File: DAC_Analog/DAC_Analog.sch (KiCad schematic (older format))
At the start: 17 parts

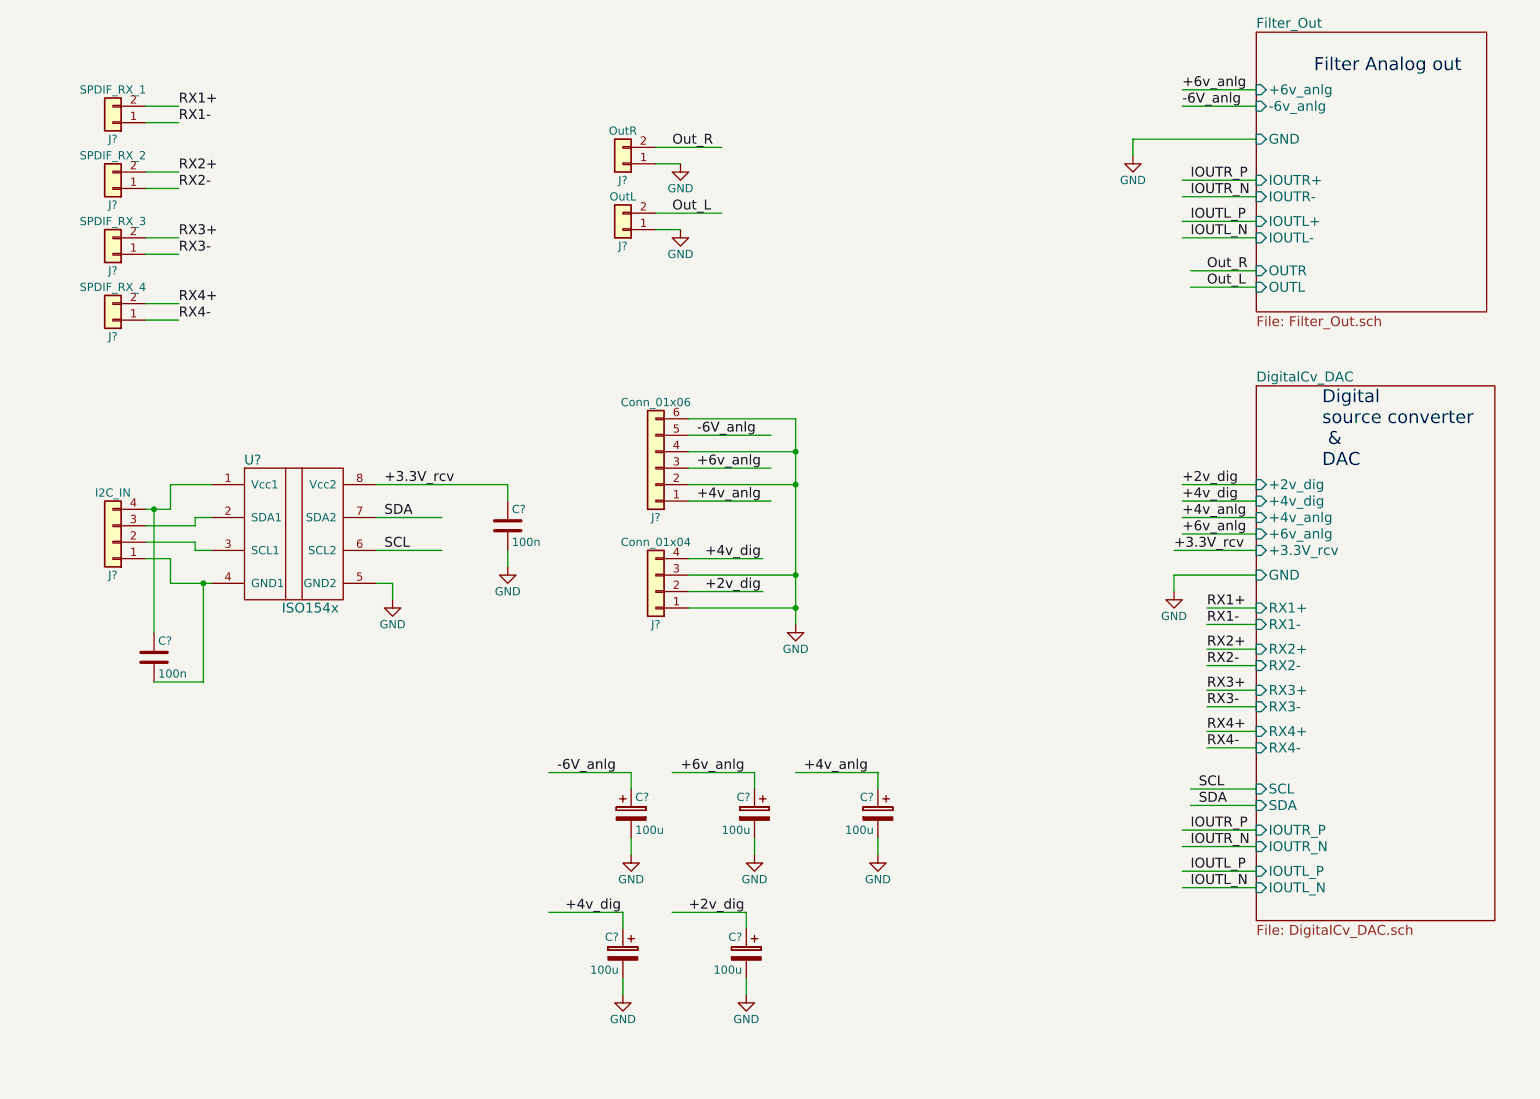
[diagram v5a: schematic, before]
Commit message: Footprint assignment ok
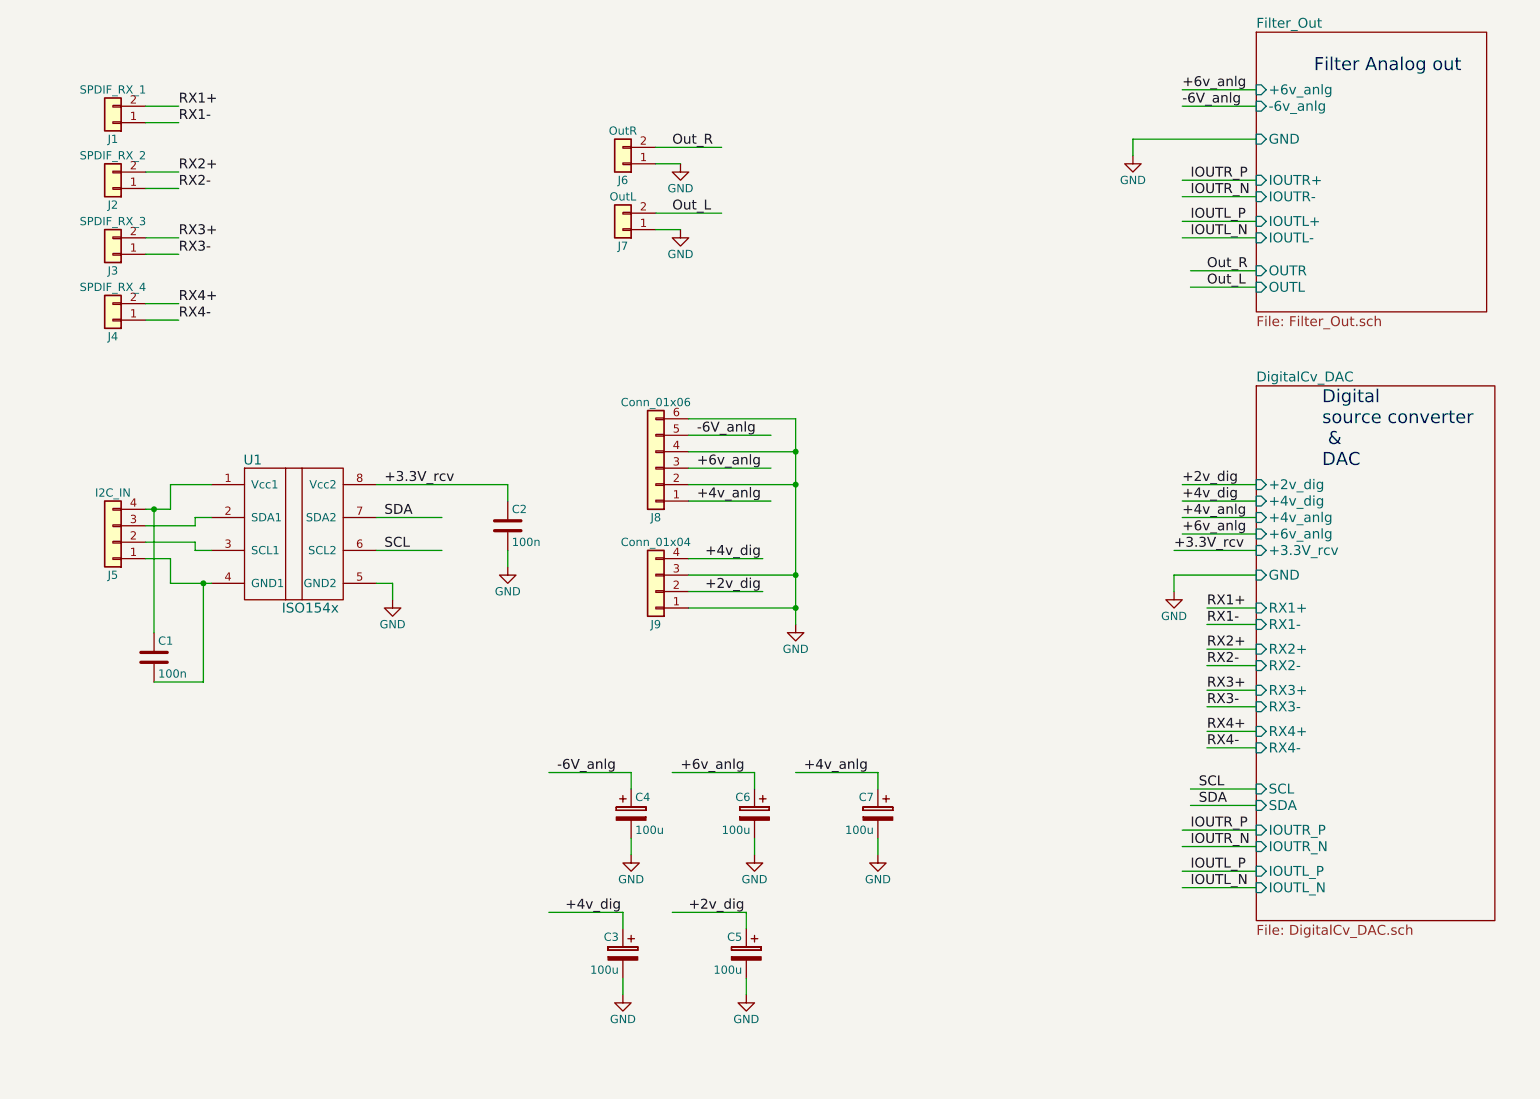
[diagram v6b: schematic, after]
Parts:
- J1, J2, J3, J4: renamed from J?; footprint (none) -> Yame_library:HE10_14-2C-2.54-MR
- J6: renamed from J?; footprint Housings_DIP:DIP-6_W10.16mm_LongPads -> Yame_library:HE10_14-2C-2.54-MR
- gave numbers to parts that had none: 12
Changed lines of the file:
@@
 Digital \nsource converter\n &\nDAC
 $Comp
-L ISO154x U?
+L ISO154x U1
 U 1 1 59C5CEDC
 P 2400 3750
-F 0 "U?" H 2150 4200 60  0000 C CNN
+F 0 "U1" H 2150 4200 60  0000 C CNN
 F 1 "ISO154x" H 2500 3300 60  0000 C CNN
 F 2 "Housings_SOIC:SOIC-8_3.9x4.9mm_Pitch1.27mm" H 2400 3750 60  0001 C CNN
@@
 $EndComp
 $Comp
-L Conn_01x02 J?
+L Conn_01x02 J1
 U 1 1 59C96FBC
 P 1300 1250
-F 0 "J?" H 1300 1350 50  0000 C CNN
+F 0 "J1" H 1300 1350 50  0000 C CNN
 F 1 "SPDIF_RX_1" H 1300 1050 50  0000 C CNN
-F 2 "" H 1300 1250 50  0001 C CNN
+F 2 "Yame_library:HE10_14-2C-2.54-MR" H 1300 1250 50  0001 C CNN
 F 3 "" H 1300 1250 50  0001 C CNN
 	1    1300 1250
@@
 $EndComp
 $Comp
-L Conn_01x02 J?
+L Conn_01x02 J2
 U 1 1 59C970A3
 P 1300 1650
-F 0 "J?" H 1300 1750 50  0000 C CNN
+F 0 "J2" H 1300 1750 50  0000 C CNN
 F 1 "SPDIF_RX_2" H 1300 1450 50  0000 C CNN
-F 2 "" H 1300 1650 50  0001 C CNN
+F 2 "Yame_library:HE10_14-2C-2.54-MR" H 1300 1650 50  0001 C CNN
 F 3 "" H 1300 1650 50  0001 C CNN
 	1    1300 1650
@@
 $EndComp
 $Comp
-L Conn_01x02 J?
+L Conn_01x02 J3
 U 1 1 59C970DE
 P 1300 2050
-F 0 "J?" H 1300 2150 50  0000 C CNN
+F 0 "J3" H 1300 2150 50  0000 C CNN
 F 1 "SPDIF_RX_3" H 1300 1850 50  0000 C CNN
-F 2 "" H 1300 2050 50  0001 C CNN
+F 2 "Yame_library:HE10_14-2C-2.54-MR" H 1300 2050 50  0001 C CNN
 F 3 "" H 1300 2050 50  0001 C CNN
 	1    1300 2050
@@
 $EndComp
 $Comp
-L Conn_01x02 J?
+L Conn_01x02 J4
 U 1 1 59C97110
 P 1300 2450
-F 0 "J?" H 1300 2550 50  0000 C CNN
+F 0 "J4" H 1300 2550 50  0000 C CNN
 F 1 "SPDIF_RX_4" H 1300 2250 50  0000 C CNN
-F 2 "" H 1300 2450 50  0001 C CNN
+F 2 "Yame_library:HE10_14-2C-2.54-MR" H 1300 2450 50  0001 C CNN
 F 3 "" H 1300 2450 50  0001 C CNN
 	1    1300 2450
@@
 $EndComp
 $Comp
-L Conn_01x04 J?
+L Conn_01x04 J9
 U 1 1 59C971D1
 P 4600 4100
-F 0 "J?" H 4600 4300 50  0000 C CNN
+F 0 "J9" H 4600 4300 50  0000 C CNN
 F 1 "Conn_01x04" H 4600 3800 50  0000 C CNN
 F 2 "Yame_library:HE10_14-4C-2.54-MR" H 4600 4100 50  0001 C CNN
@@
 $EndComp
 $Comp
-L Conn_01x06 J?
+L Conn_01x06 J8
 U 1 1 59C972F4
 P 4600 3350
-F 0 "J?" H 4600 3650 50  0000 C CNN
+F 0 "J8" H 4600 3650 50  0000 C CNN
 F 1 "Conn_01x06" H 4600 2950 50  0000 C CNN
 F 2 "Yame_library:HE10_14-6C-2.54-MR" H 4600 3350 50  0001 C CNN
@@
 $EndComp
 $Comp
-L Conn_01x04 J?
+L Conn_01x04 J5
 U 1 1 59C97424
 P 1300 3800
-F 0 "J?" H 1300 4000 50  0000 C CNN
+F 0 "J5" H 1300 4000 50  0000 C CNN
 F 1 "I2C_IN" H 1300 3500 50  0000 C CNN
 F 2 "Yame_library:HE10_14-4C-2.54-MR" H 1300 3800 50  0001 C CNN
@@
 $EndComp
 $Comp
-L Conn_01x02 J?
+L Conn_01x02 J6
 U 1 1 59C976CC
 P 4400 1500
-F 0 "J?" H 4400 1600 50  0000 C CNN
+F 0 "J6" H 4400 1600 50  0000 C CNN
 F 1 "OutR" H 4400 1300 50  0000 C CNN
-F 2 "Housings_DIP:DIP-6_W10.16mm_LongPads" H 4400 1500 50  0001 C CNN
+F 2 "Yame_library:HE10_14-2C-2.54-MR" H 4400 1500 50  0001 C CNN
 F 3 "" H 4400 1500 50  0001 C CNN
 	1    4400 1500
@@
 $EndComp
 $Comp
-L Conn_01x02 J?
+L Conn_01x02 J7
 U 1 1 59C976D2
 P 4400 1900
-F 0 "J?" H 4400 2000 50  0000 C CNN
+F 0 "J7" H 4400 2000 50  0000 C CNN
 F 1 "OutL" H 4400 1700 50  0000 C CNN
 F 2 "Yame_library:HE10_14-2C-2.54-MR" H 4400 1900 50  0001 C CNN
@@
 	1650 4050 1900 4050
 $Comp
-L GND #PWR?
+L GND #PWR01
 U 1 1 59CB983A
 P 3000 4150
-F 0 "#PWR?" H 3000 3900 50  0001 C CNN
+F 0 "#PWR01" H 3000 3900 50  0001 C CNN
 F 1 "GND" H 3000 4000 50  0000 C CNN
 F 2 "" H 3000 4150 50  0001 C CNN
@@
 	7850 2250 8250 2250
 $Comp
-L GND #PWR?
+L GND #PWR02
 U 1 1 59CBC1FC
 P 7750 4100
-F 0 "#PWR?" H 7750 3850 50  0001 C CNN
+F 0 "#PWR02" H 7750 3850 50  0001 C CNN
 F 1 "GND" H 7750 3950 50  0000 C CNN
 F 2 "" H 7750 4100 50  0001 C CNN
@@
 	7750 4000 7750 4100
 $Comp
-L GND #PWR?
+L GND #PWR03
 U 1 1 59CBC549
 P 7500 1450
-F 0 "#PWR?" H 7500 1200 50  0001 C CNN
+F 0 "#PWR03" H 7500 1200 50  0001 C CNN
 F 1 "GND" H 7500 1300 50  0000 C CNN
 F 2 "" H 7500 1450 50  0001 C CNN
@@
 	4600 1800 5000 1800
 $Comp
-L GND #PWR?
+L GND #PWR04
 U 1 1 59CBD970
 P 4750 1500
-F 0 "#PWR?" H 4750 1250 50  0001 C CNN
+F 0 "#PWR04" H 4750 1250 50  0001 C CNN
 F 1 "GND" H 4750 1350 50  0000 C CNN
 F 2 "" H 4750 1500 50  0001 C CNN
@@
 $EndComp
 $Comp
-L GND #PWR?
+L GND #PWR05
 U 1 1 59CBD9E8
 P 4750 1900
-F 0 "#PWR?" H 4750 1650 50  0001 C CNN
+F 0 "#PWR05" H 4750 1650 50  0001 C CNN
 F 1 "GND" H 4750 1750 50  0000 C CNN
 F 2 "" H 4750 1900 50  0001 C CNN
@@
 Connection ~ 5450 4200
 $Comp
-L C C?
+L C C2
 U 1 1 59CC79C1
 P 3700 3700
-F 0 "C?" H 3725 3800 50  0000 L CNN
+F 0 "C2" H 3725 3800 50  0000 L CNN
 F 1 "100n" H 3725 3600 50  0000 L CNN
 F 2 "Yame_library:SM0603-MR" H 3738 3550 50  0001 C CNN
@@
 $EndComp
 $Comp
-L C C?
+L C C1
 U 1 1 59CC7D14
 P 1550 4500
-F 0 "C?" H 1575 4600 50  0000 L CNN
+F 0 "C1" H 1575 4600 50  0000 L CNN
 F 1 "100n" H 1575 4400 50  0000 L CNN
 F 2 "Yame_library:SM0603-MR" H 1588 4350 50  0001 C CNN
@@
 	3700 3450 3700 3550
 $Comp
-L GND #PWR?
+L GND #PWR06
 U 1 1 59CC829B
 P 3700 3950
-F 0 "#PWR?" H 3700 3700 50  0001 C CNN
+F 0 "#PWR06" H 3700 3700 50  0001 C CNN
 F 1 "GND" H 3700 3800 50  0000 C CNN
 F 2 "" H 3700 3950 50  0001 C CNN
@@
 -6V_anlg
 $Comp
-L CP C?
+L CP C4
 U 1 1 59CC96F6
 P 4450 5450
-F 0 "C?" H 4475 5550 50  0000 L CNN
+F 0 "C4" H 4475 5550 50  0000 L CNN
 F 1 "100u" H 4475 5350 50  0000 L CNN
 F 2 "Capacitors_THT:CP_Radial_Tantal_D8.0mm_P2.50mm" H 4488 5300 50  0001 C CNN
@@
 $EndComp
 $Comp
-L CP C?
+L CP C6
 U 1 1 59CCA036
 P 5200 5450
-F 0 "C?" H 5225 5550 50  0000 L CNN
+F 0 "C6" H 5225 5550 50  0000 L CNN
 F 1 "100u" H 5225 5350 50  0000 L CNN
 F 2 "Capacitors_THT:CP_Radial_Tantal_D8.0mm_P2.50mm" H 5238 5300 50  0001 C CNN
@@
 $EndComp
 $Comp
-L CP C?
+L CP C7
 U 1 1 59CCA13A
 P 5950 5450
-F 0 "C?" H 5975 5550 50  0000 L CNN
+F 0 "C7" H 5975 5550 50  0000 L CNN
 F 1 "100u" H 5975 5350 50  0000 L CNN
 F 2 "Capacitors_THT:CP_Radial_Tantal_D8.0mm_P2.50mm" H 5988 5300 50  0001 C CNN
@@
 $EndComp
 $Comp
-L CP C?
+L CP C5
 U 1 1 59CCA245
 P 5150 6300
-F 0 "C?" H 5175 6400 50  0000 L CNN
+F 0 "C5" H 5175 6400 50  0000 L CNN
 F 1 "100u" H 5175 6200 50  0000 L CNN
 F 2 "Capacitors_THT:CP_Radial_Tantal_D8.0mm_P2.50mm" H 5188 6150 50  0001 C CNN
@@
 $EndComp
 $Comp
-L CP C?
+L CP C3
 U 1 1 59CCA371
 P 4400 6300
-F 0 "C?" H 4425 6400 50  0000 L CNN
+F 0 "C3" H 4425 6400 50  0000 L CNN
 F 1 "100u" H 4425 6200 50  0000 L CNN
 F 2 "Capacitors_THT:CP_Radial_Tantal_D8.0mm_P2.50mm" H 4438 6150 50  0001 C CNN
@@
 $EndComp
 $Comp
-L GND #PWR?
+L GND #PWR07
 U 1 1 59CC3026
 P 5450 4300
-F 0 "#PWR?" H 5450 4050 50  0001 C CNN
+F 0 "#PWR07" H 5450 4050 50  0001 C CNN
 F 1 "GND" H 5450 4150 50  0000 C CNN
 F 2 "" H 5450 4300 50  0001 C CNN
@@
 $EndComp
 $Comp
-L GND #PWR?
+L GND #PWR08
 U 1 1 59CCA544
 P 4450 5700
-F 0 "#PWR?" H 4450 5450 50  0001 C CNN
+F 0 "#PWR08" H 4450 5450 50  0001 C CNN
 F 1 "GND" H 4450 5550 50  0000 C CNN
 F 2 "" H 4450 5700 50  0001 C CNN
@@
 $EndComp
 $Comp
-L GND #PWR?
+L GND #PWR09
 U 1 1 59CCA62A
 P 5200 5700
-F 0 "#PWR?" H 5200 5450 50  0001 C CNN
+F 0 "#PWR09" H 5200 5450 50  0001 C CNN
 F 1 "GND" H 5200 5550 50  0000 C CNN
 F 2 "" H 5200 5700 50  0001 C CNN
@@
 $EndComp
 $Comp
-L GND #PWR?
+L GND #PWR010
 U 1 1 59CCA710
 P 5950 5700
-F 0 "#PWR?" H 5950 5450 50  0001 C CNN
+F 0 "#PWR010" H 5950 5450 50  0001 C CNN
 F 1 "GND" H 5950 5550 50  0000 C CNN
 F 2 "" H 5950 5700 50  0001 C CNN
@@
 $EndComp
 $Comp
-L GND #PWR?
+L GND #PWR011
 U 1 1 59CCA7F6
 P 5150 6550
-F 0 "#PWR?" H 5150 6300 50  0001 C CNN
+F 0 "#PWR011" H 5150 6300 50  0001 C CNN
 F 1 "GND" H 5150 6400 50  0000 C CNN
 F 2 "" H 5150 6550 50  0001 C CNN
@@
 $EndComp
 $Comp
-L GND #PWR?
+L GND #PWR012
 U 1 1 59CCA8DC
 P 4400 6550
-F 0 "#PWR?" H 4400 6300 50  0001 C CNN
+F 0 "#PWR012" H 4400 6300 50  0001 C CNN
 F 1 "GND" H 4400 6400 50  0000 C CNN
 F 2 "" H 4400 6550 50  0001 C CNN

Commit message: update footprint
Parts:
- J1, J2, J3, J4, J6, J7: footprint Yame_library:HE10_14-2C-2.54-MR -> Pin_Headers:Pin_Header_Straight_1x02_Pitch2.54mm
- J5, J9: footprint Yame_library:HE10_14-4C-2.54-MR -> Pin_Headers:Pin_Header_Straight_1x04_Pitch2.54mm
- J8: footprint Yame_library:HE10_14-6C-2.54-MR -> Pin_Headers:Pin_Header_Straight_1x06_Pitch2.54mm
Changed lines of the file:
@@
 F 0 "J1" H 1300 1350 50  0000 C CNN
 F 1 "SPDIF_RX_1" H 1300 1050 50  0000 C CNN
-F 2 "Yame_library:HE10_14-2C-2.54-MR" H 1300 1250 50  0001 C CNN
+F 2 "Pin_Headers:Pin_Header_Straight_1x02_Pitch2.54mm" H 1300 1250 50  0001 C CNN
 F 3 "" H 1300 1250 50  0001 C CNN
 	1    1300 1250
@@
 F 0 "J2" H 1300 1750 50  0000 C CNN
 F 1 "SPDIF_RX_2" H 1300 1450 50  0000 C CNN
-F 2 "Yame_library:HE10_14-2C-2.54-MR" H 1300 1650 50  0001 C CNN
+F 2 "Pin_Headers:Pin_Header_Straight_1x02_Pitch2.54mm" H 1300 1650 50  0001 C CNN
 F 3 "" H 1300 1650 50  0001 C CNN
 	1    1300 1650
@@
 F 0 "J3" H 1300 2150 50  0000 C CNN
 F 1 "SPDIF_RX_3" H 1300 1850 50  0000 C CNN
-F 2 "Yame_library:HE10_14-2C-2.54-MR" H 1300 2050 50  0001 C CNN
+F 2 "Pin_Headers:Pin_Header_Straight_1x02_Pitch2.54mm" H 1300 2050 50  0001 C CNN
 F 3 "" H 1300 2050 50  0001 C CNN
 	1    1300 2050
@@
 F 0 "J4" H 1300 2550 50  0000 C CNN
 F 1 "SPDIF_RX_4" H 1300 2250 50  0000 C CNN
-F 2 "Yame_library:HE10_14-2C-2.54-MR" H 1300 2450 50  0001 C CNN
+F 2 "Pin_Headers:Pin_Header_Straight_1x02_Pitch2.54mm" H 1300 2450 50  0001 C CNN
 F 3 "" H 1300 2450 50  0001 C CNN
 	1    1300 2450
@@
 F 0 "J9" H 4600 4300 50  0000 C CNN
 F 1 "Conn_01x04" H 4600 3800 50  0000 C CNN
-F 2 "Yame_library:HE10_14-4C-2.54-MR" H 4600 4100 50  0001 C CNN
+F 2 "Pin_Headers:Pin_Header_Straight_1x04_Pitch2.54mm" H 4600 4100 50  0001 C CNN
 F 3 "" H 4600 4100 50  0001 C CNN
 	1    4600 4100
@@
 F 0 "J8" H 4600 3650 50  0000 C CNN
 F 1 "Conn_01x06" H 4600 2950 50  0000 C CNN
-F 2 "Yame_library:HE10_14-6C-2.54-MR" H 4600 3350 50  0001 C CNN
+F 2 "Pin_Headers:Pin_Header_Straight_1x06_Pitch2.54mm" H 4600 3350 50  0001 C CNN
 F 3 "" H 4600 3350 50  0001 C CNN
 	1    4600 3350
@@
 F 0 "J5" H 1300 4000 50  0000 C CNN
 F 1 "I2C_IN" H 1300 3500 50  0000 C CNN
-F 2 "Yame_library:HE10_14-4C-2.54-MR" H 1300 3800 50  0001 C CNN
+F 2 "Pin_Headers:Pin_Header_Straight_1x04_Pitch2.54mm" H 1300 3800 50  0001 C CNN
 F 3 "" H 1300 3800 50  0001 C CNN
 	1    1300 3800
@@
 F 0 "J6" H 4400 1600 50  0000 C CNN
 F 1 "OutR" H 4400 1300 50  0000 C CNN
-F 2 "Yame_library:HE10_14-2C-2.54-MR" H 4400 1500 50  0001 C CNN
+F 2 "Pin_Headers:Pin_Header_Straight_1x02_Pitch2.54mm" H 4400 1500 50  0001 C CNN
 F 3 "" H 4400 1500 50  0001 C CNN
 	1    4400 1500
@@
 F 0 "J7" H 4400 2000 50  0000 C CNN
 F 1 "OutL" H 4400 1700 50  0000 C CNN
-F 2 "Yame_library:HE10_14-2C-2.54-MR" H 4400 1900 50  0001 C CNN
+F 2 "Pin_Headers:Pin_Header_Straight_1x02_Pitch2.54mm" H 4400 1900 50  0001 C CNN
 F 3 "" H 4400 1900 50  0001 C CNN
 	1    4400 1900

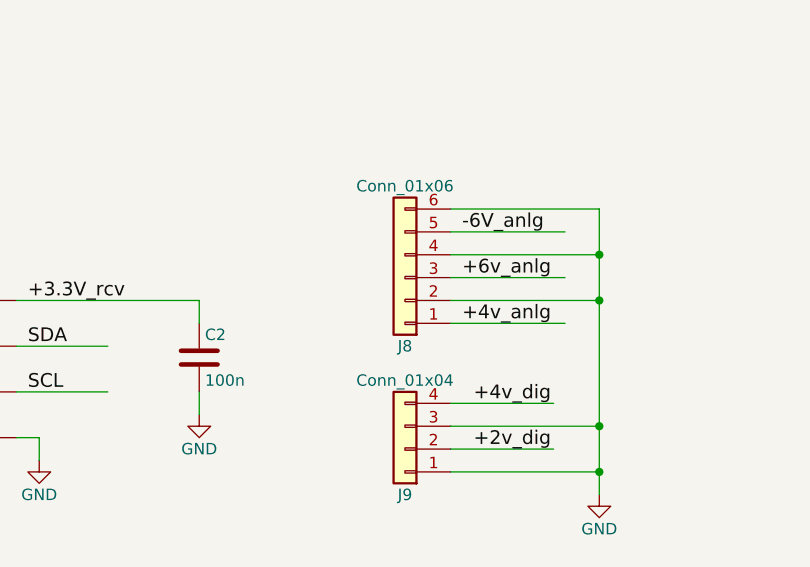
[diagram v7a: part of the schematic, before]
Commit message: place all components on DAC_Analog
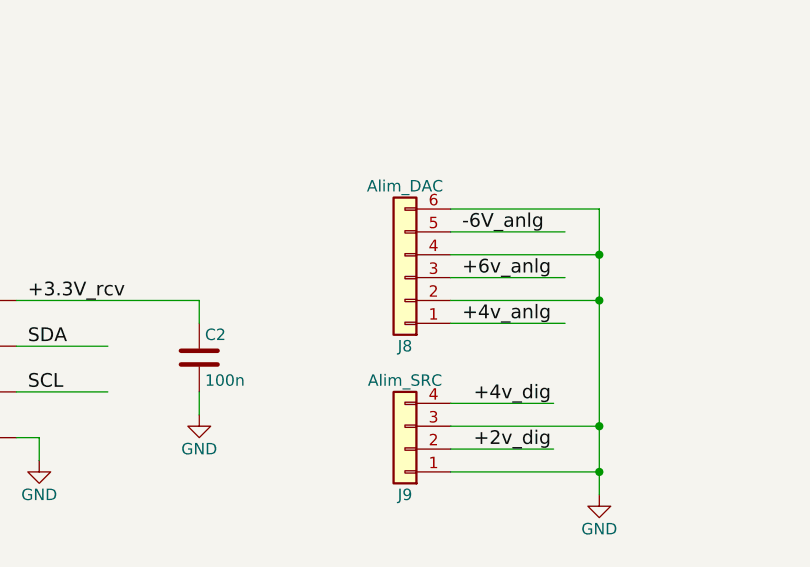
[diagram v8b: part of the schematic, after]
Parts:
- J8: value Conn_01x06 -> Alim_DAC
- J9: value Conn_01x04 -> Alim_SRC
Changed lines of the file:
@@
 P 4600 4100
 F 0 "J9" H 4600 4300 50  0000 C CNN
-F 1 "Conn_01x04" H 4600 3800 50  0000 C CNN
+F 1 "Alim_SRC" H 4600 3800 50  0000 C CNN
 F 2 "Pin_Headers:Pin_Header_Straight_1x04_Pitch2.54mm" H 4600 4100 50  0001 C CNN
 F 3 "" H 4600 4100 50  0001 C CNN
@@
 P 4600 3350
 F 0 "J8" H 4600 3650 50  0000 C CNN
-F 1 "Conn_01x06" H 4600 2950 50  0000 C CNN
+F 1 "Alim_DAC" H 4600 2950 50  0000 C CNN
 F 2 "Pin_Headers:Pin_Header_Straight_1x06_Pitch2.54mm" H 4600 3350 50  0001 C CNN
 F 3 "" H 4600 3350 50  0001 C CNN
